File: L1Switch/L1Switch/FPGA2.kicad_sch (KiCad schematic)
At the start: 9 parts, among them J10 Conn_02x07_Odd_Even, U1 XC7A35T-FTG256, U10 W25Q128JVS, U11 TXB0108PW

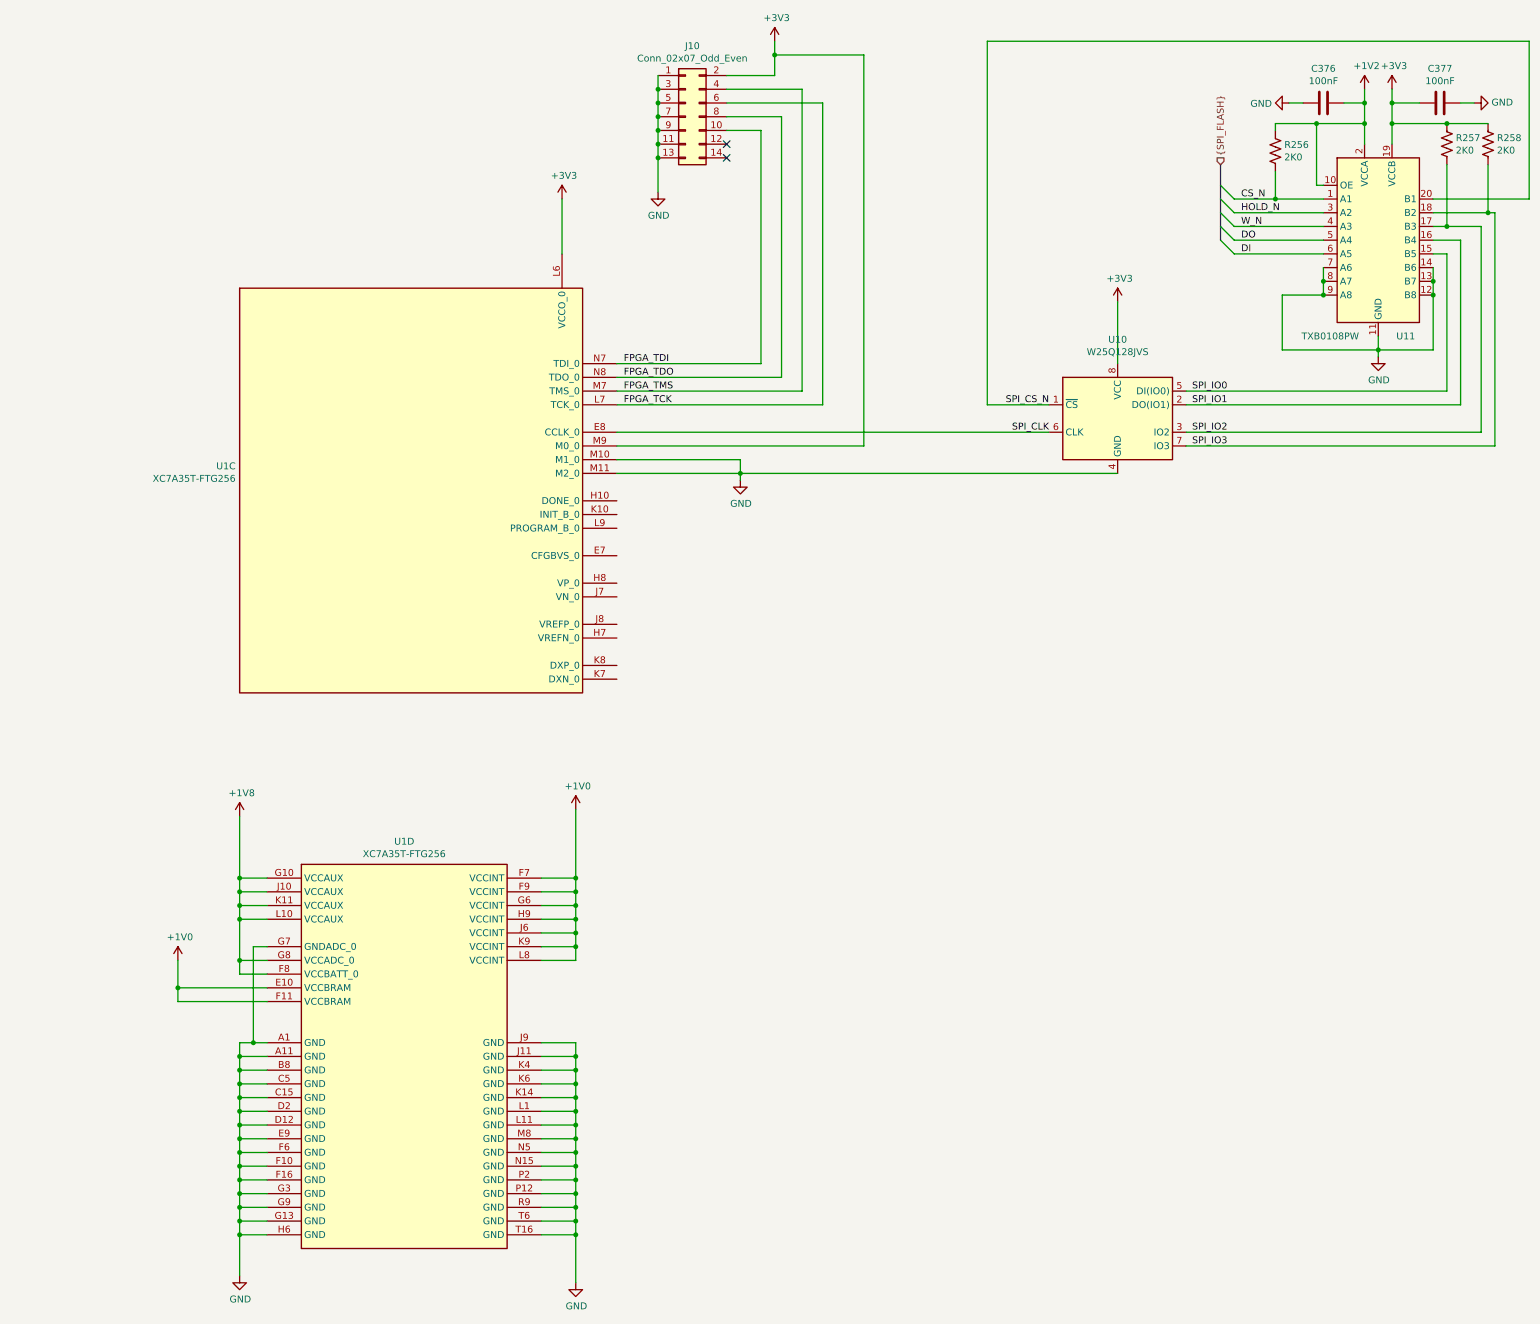
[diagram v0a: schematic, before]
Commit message: Added power-on-reset circuit.
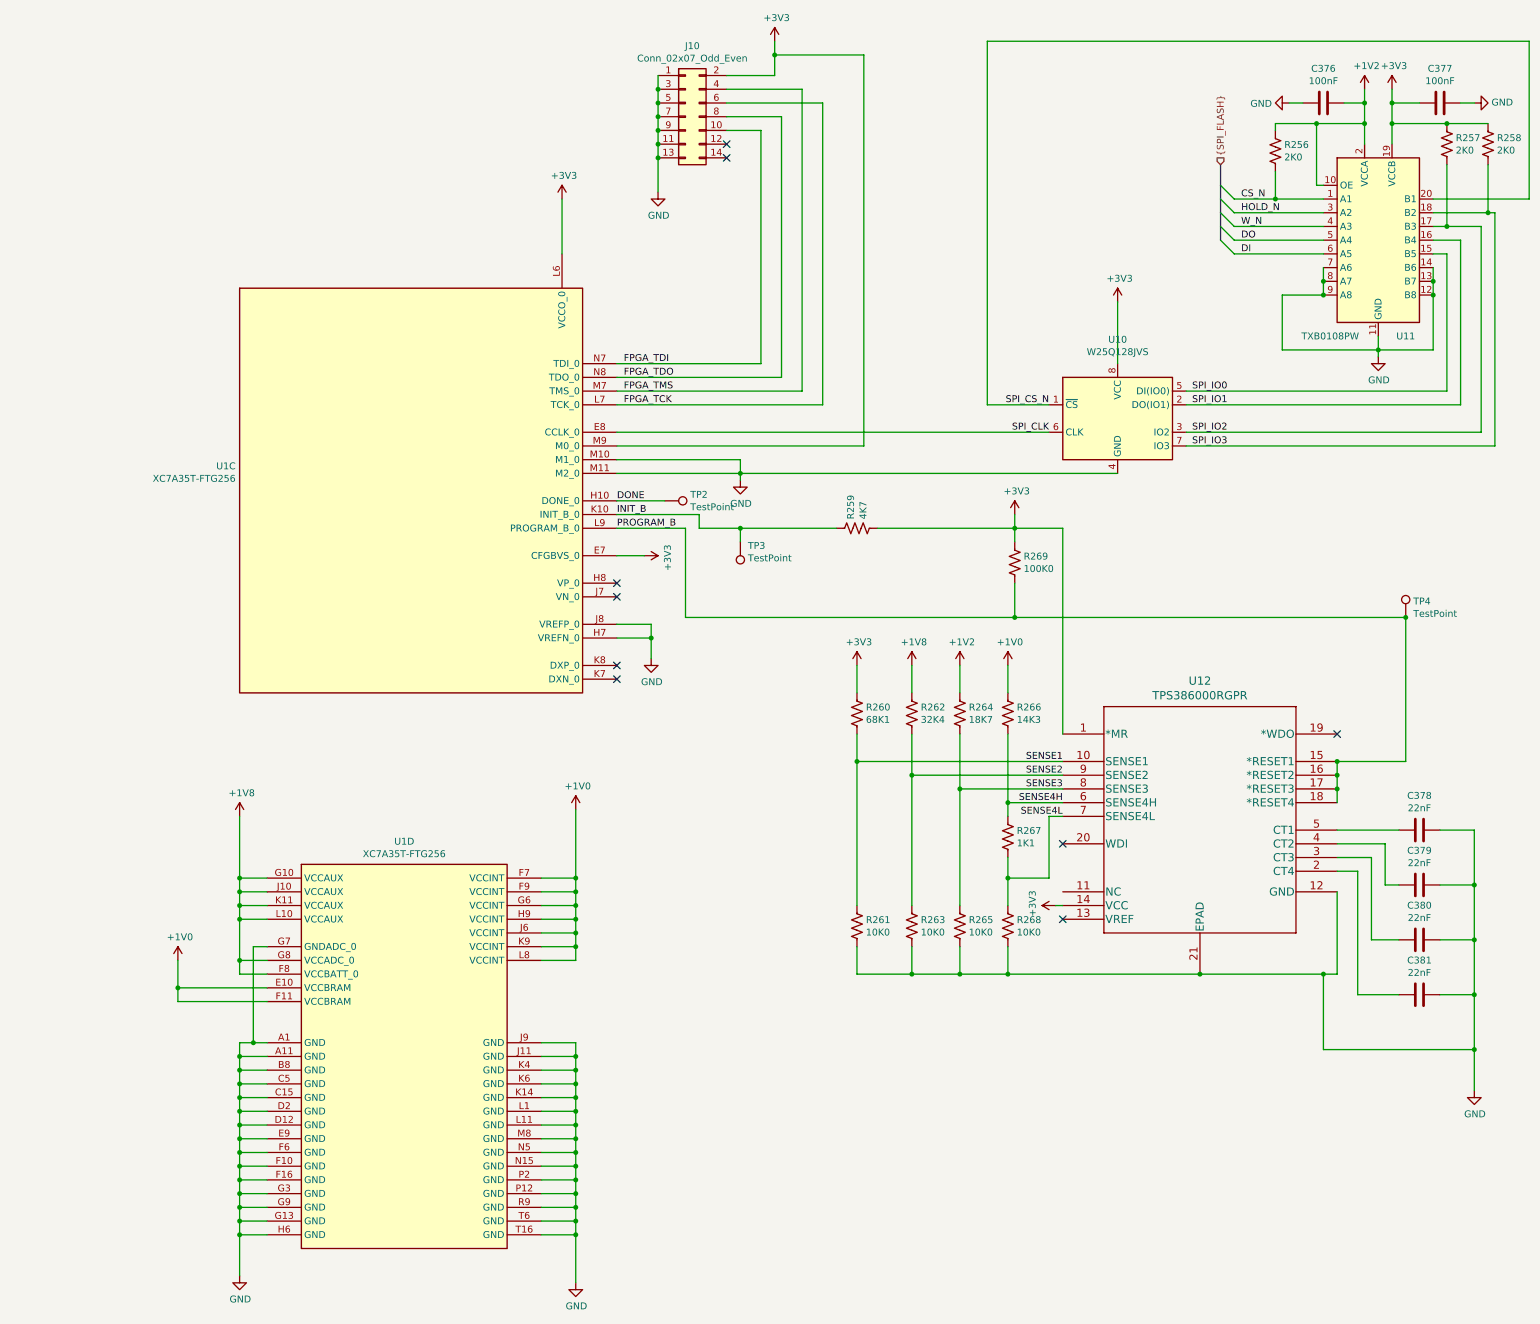
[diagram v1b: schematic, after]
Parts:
- added C378, C379, C380, C381: 22nF, Capacitor_SMD:C_0402_1005Metric, symbol Device:C
- added R259: 4K7, Resistor_SMD:R_0402_1005Metric, symbol Device:R_US
- added R260: 68K1, Resistor_SMD:R_0402_1005Metric, symbol Device:R_US
- added R261, R263, R265, R268: 10K0, Resistor_SMD:R_0402_1005Metric, symbol Device:R_US
- added R262: 32K4, Resistor_SMD:R_0402_1005Metric, symbol Device:R_US
- added R264: 18K7, Resistor_SMD:R_0402_1005Metric, symbol Device:R_US
- added R266: 14K3, Resistor_SMD:R_0402_1005Metric, symbol Device:R_US
- added R267: 1K1, Resistor_SMD:R_0402_1005Metric, symbol Device:R_US
- added R269: 100K0, Resistor_SMD:R_0402_1005Metric, symbol Device:R_US
- added TP2, TP3, TP4: TestPoint, TestPoint:TestPoint_Pad_1.0x1.0mm, symbol Connector:TestPoint
- added U12: TPS386000RGPR, L1Switch:TPS386000RGPR, symbol L1Switch:TPS386000RGPR
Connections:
- net +1V0: now also R266.1
- net +1V2: now also R264.1
- net +1V8: now also R262.1
- net +3V3: now also U1.E7 (CFGBVS_0), R259.2, R260.1, R269.1, U12.1 (*MR), U12.14 (VCC)
- net GND: now also U1.H7 (VREFN_0), U1.J8 (VREFP_0), C378.2, C379.2, C380.2, C381.2, R261.2, R263.2, R265.2, R268.2, U12.12 (GND), U12.21 (EPAD)
- net DONE: now reaches U1.H10 (DONE_0)
- net DONE: now also TP2.1
- net INIT_B: now reaches U1.K10 (INIT_B_0)
- net INIT_B: now also R259.1, TP3.1
- net PROGRAM_B: now reaches U1.L9 (PROGRAM_B_0)
- net PROGRAM_B: now also R269.2, TP4.1, U12.15 (*RESET1), U12.16 (*RESET2), U12.17 (*RESET3), U12.18 (*RESET4)
- new net: C378.1, U12.5 (CT1)
- new net: C379.1, U12.4 (CT2)
- new net: C381.1, U12.2 (CT4)
- new net: C380.1, U12.3 (CT3)
- new net SENSE1: R260.2, R261.1, U12.10 (SENSE1)
- new net SENSE2: R262.2, R263.1, U12.9 (SENSE2)
- new net SENSE3: R264.2, R265.1, U12.8 (SENSE3)
- new net SENSE4H: R266.2, R267.1, U12.6 (SENSE4H)
- new net SENSE4L: R267.2, R268.1, U12.7 (SENSE4L)
- no-connect marks 2 -> 9

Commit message: Add FPGA decoupling caps. Add some power planes.
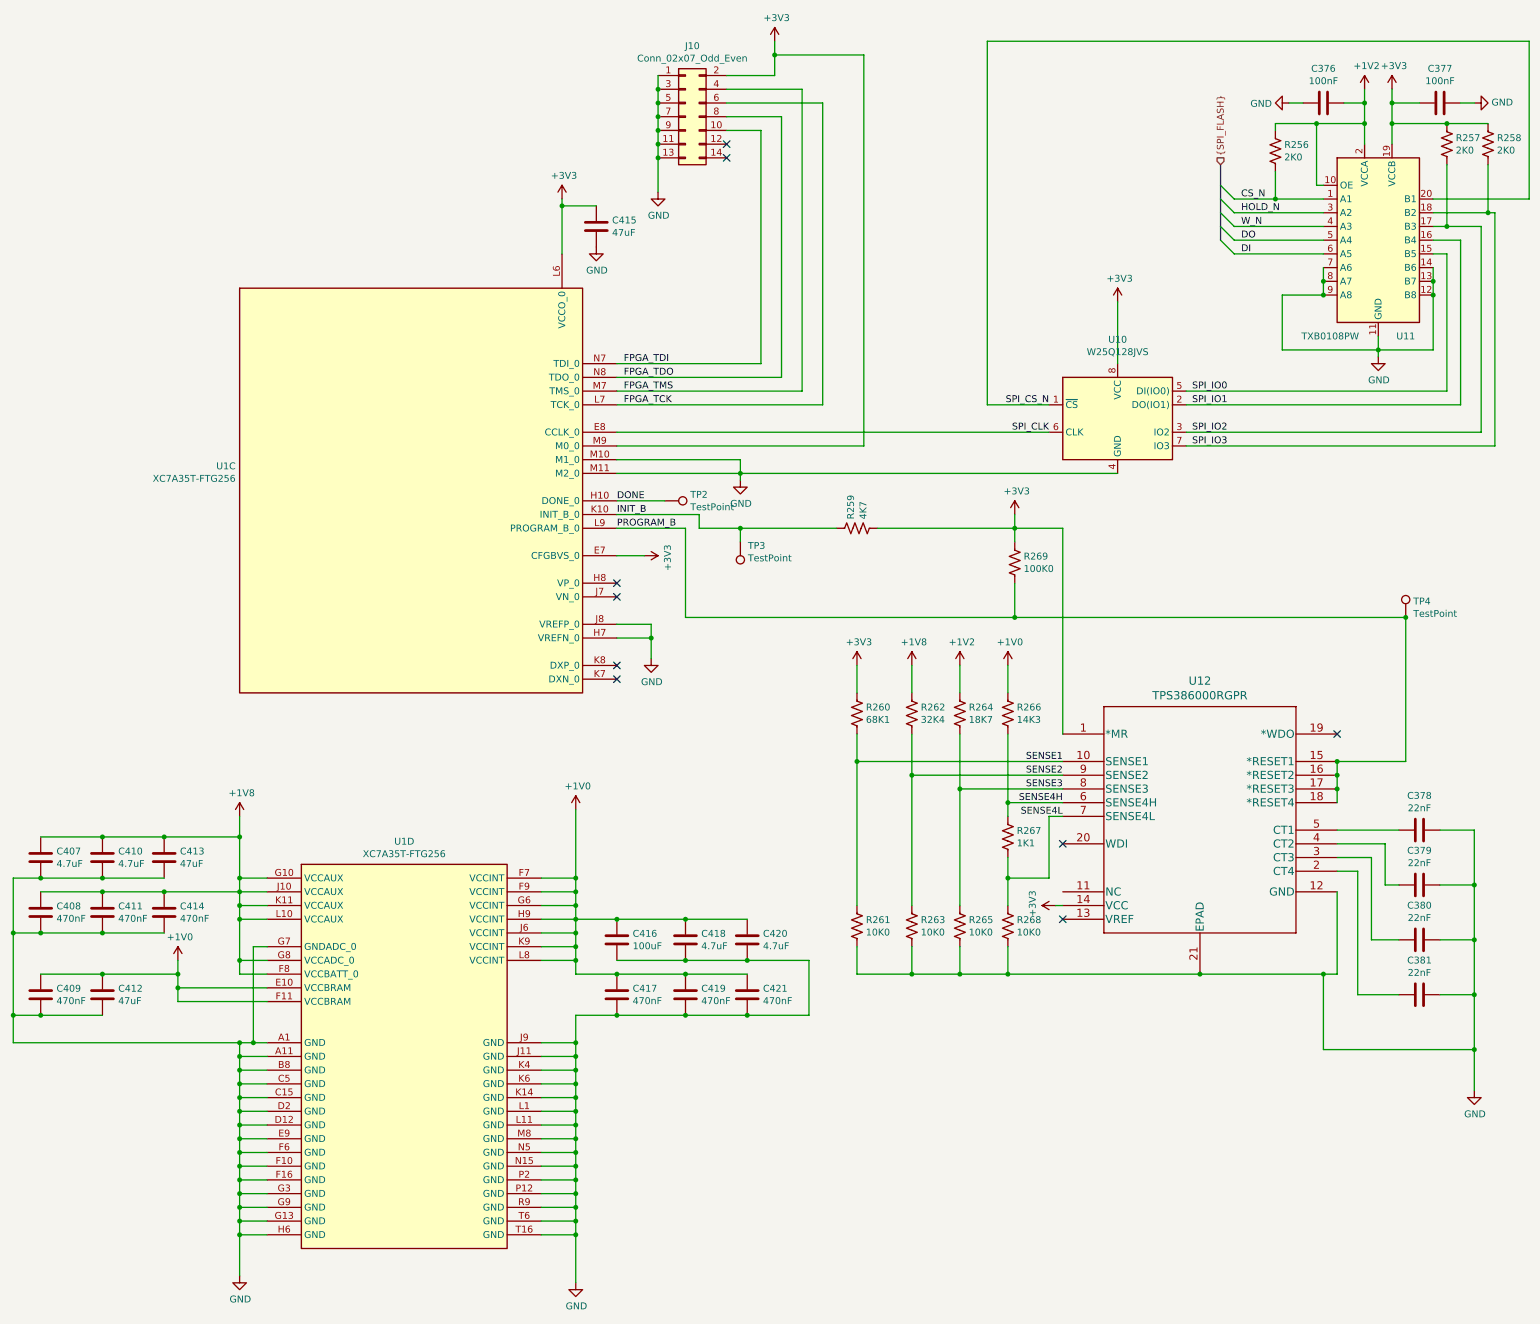
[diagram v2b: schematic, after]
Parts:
- added C407, C410, C418, C420: 4.7uF, Capacitor_SMD:C_0805_2012Metric, symbol Device:C
- added C408, C409, C411, C414, C417, C419, C421: 470nF, Capacitor_SMD:C_0402_1005Metric, symbol Device:C
- added C412, C413, C415: 47uF, Capacitor_SMD:C_1210_3225Metric, symbol Device:C
- added C416: 100uF, Capacitor_SMD:C_1210_3225Metric, symbol Device:C
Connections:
- net +1V0: now also C409.1, C412.1, C416.1, C417.1, C418.1, C419.1, C420.1, C421.1
- net +1V8: now also C407.1, C408.1, C410.1, C411.1, C413.1, C414.1
- net +3V3: now also C415.1
- net GND: now also C407.2, C408.2, C409.2, C410.2, C411.2, C412.2, C413.2, C414.2, C415.2, C416.2, C417.2, C418.2, C419.2, C420.2, C421.2

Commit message: Add some part info. Fix footprint size for 2kV caps. Add a plane cutout around the magnetics.
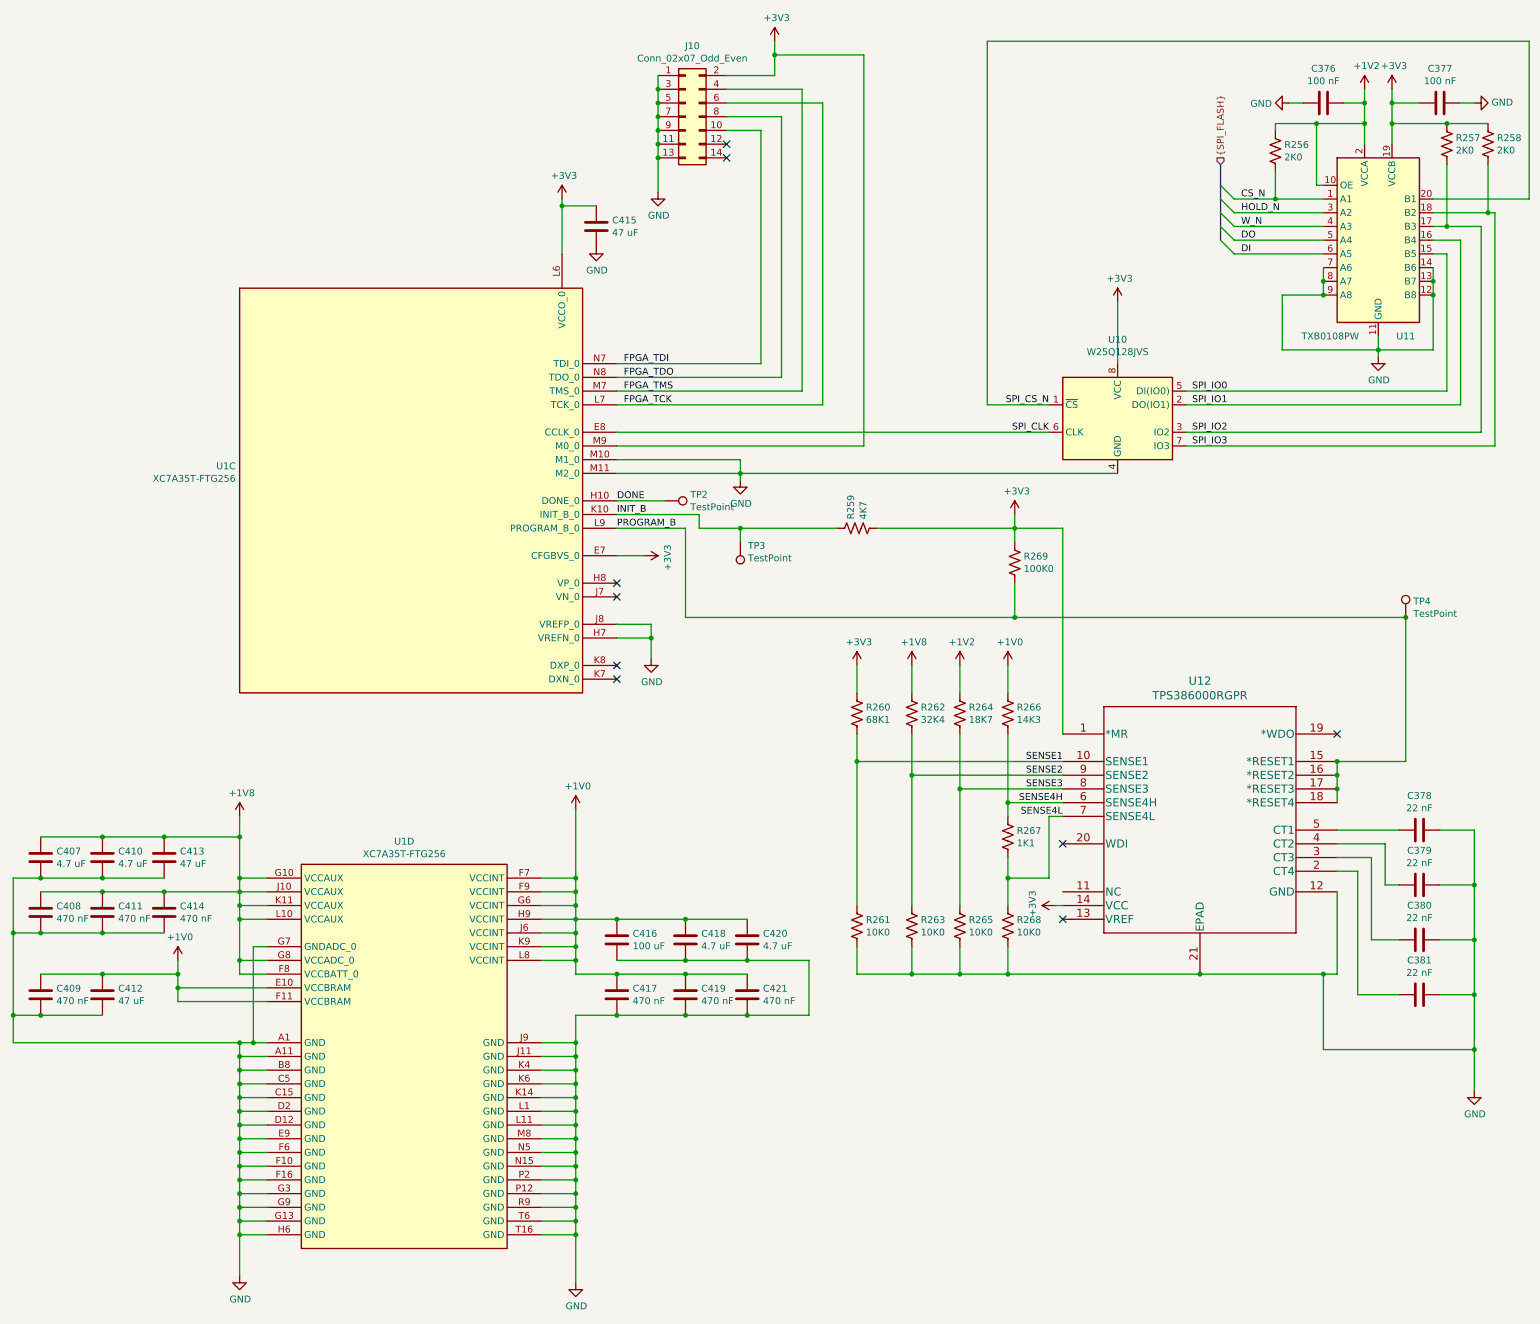
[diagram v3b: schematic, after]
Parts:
- C376, C377: value 100nF -> 100 nF; MFR Part# (none) -> GRM155R71C104KA57D; Manufacturer (none) -> MuRata
- C378, C379, C380, C381: value 22nF -> 22 nF; MFR Part# (none) -> EMK105B7223KV-F; Manufacturer (none) -> Taiyo Yuden
- C407, C410, C418, C420: value 4.7uF -> 4.7 uF; MFR Part# (none) -> C0805C475K9PAC; Manufacturer (none) -> Kemet
- C408, C409, C411, C414, C417, C419, C421: value 470nF -> 470 nF; MFR Part# (none) -> GRM155R61C474KE01D; Manufacturer (none) -> MuRata
- C412, C413, C415: value 47uF -> 47 uF; MFR Part# (none) -> GRM32EB31A476KE20L; Manufacturer (none) -> MuRata
- C416: value 100uF -> 100 uF; MFR Part# (none) -> GRM32EC80G107KE20L; Manufacturer (none) -> MuRata
- J10: MFR Part# (none) -> 87758-1416; Manufacturer (none) -> Molex
- U1: MFR Part# (none) -> XC7A35T-2FTG256C; Manufacturer (none) -> Xilinx
- U10: MFR Part# (none) -> W25Q128JVSIM; Manufacturer (none) -> Winbond
- U11: MFR Part# (none) -> TXB0108PWR; Manufacturer (none) -> Texas Instruments
- U12: MFR Part# (none) -> TPS386000RGPR; Manufacturer (none) -> Texas Instruments
